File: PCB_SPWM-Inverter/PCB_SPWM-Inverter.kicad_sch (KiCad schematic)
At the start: 14 parts, among them J1 VAC, J2 VIN, Q1 IRFZ44NPBF, Q2 IRFZ44NPBF, Q3 IRFZ44NPBF, Q4 IRFZ44NPBF, U1 STM32F401, U2 LM2596, U3 TC4420EPA, U4 TC4420EPA, U5 TC4420EPA, U6 TC4420EPA

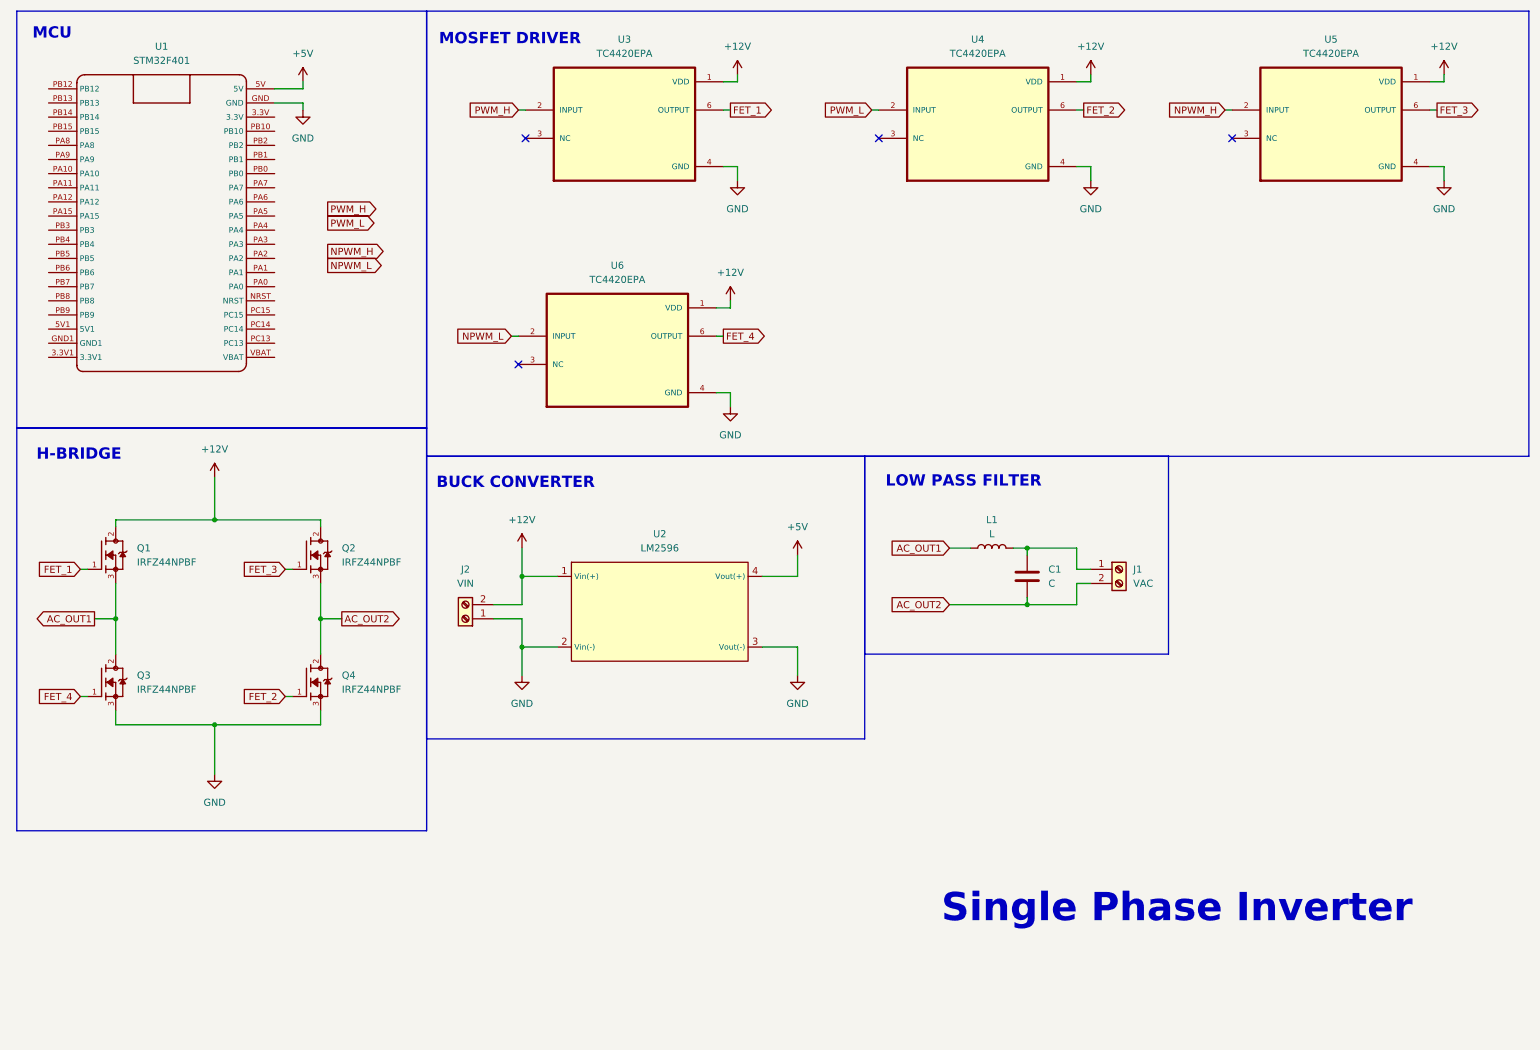
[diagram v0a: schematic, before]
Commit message: Add protection for H-bridge, calculate mosfet output, change mosfet driver to Half Bridge driver due to incompatibility on high side switching (unfinished)
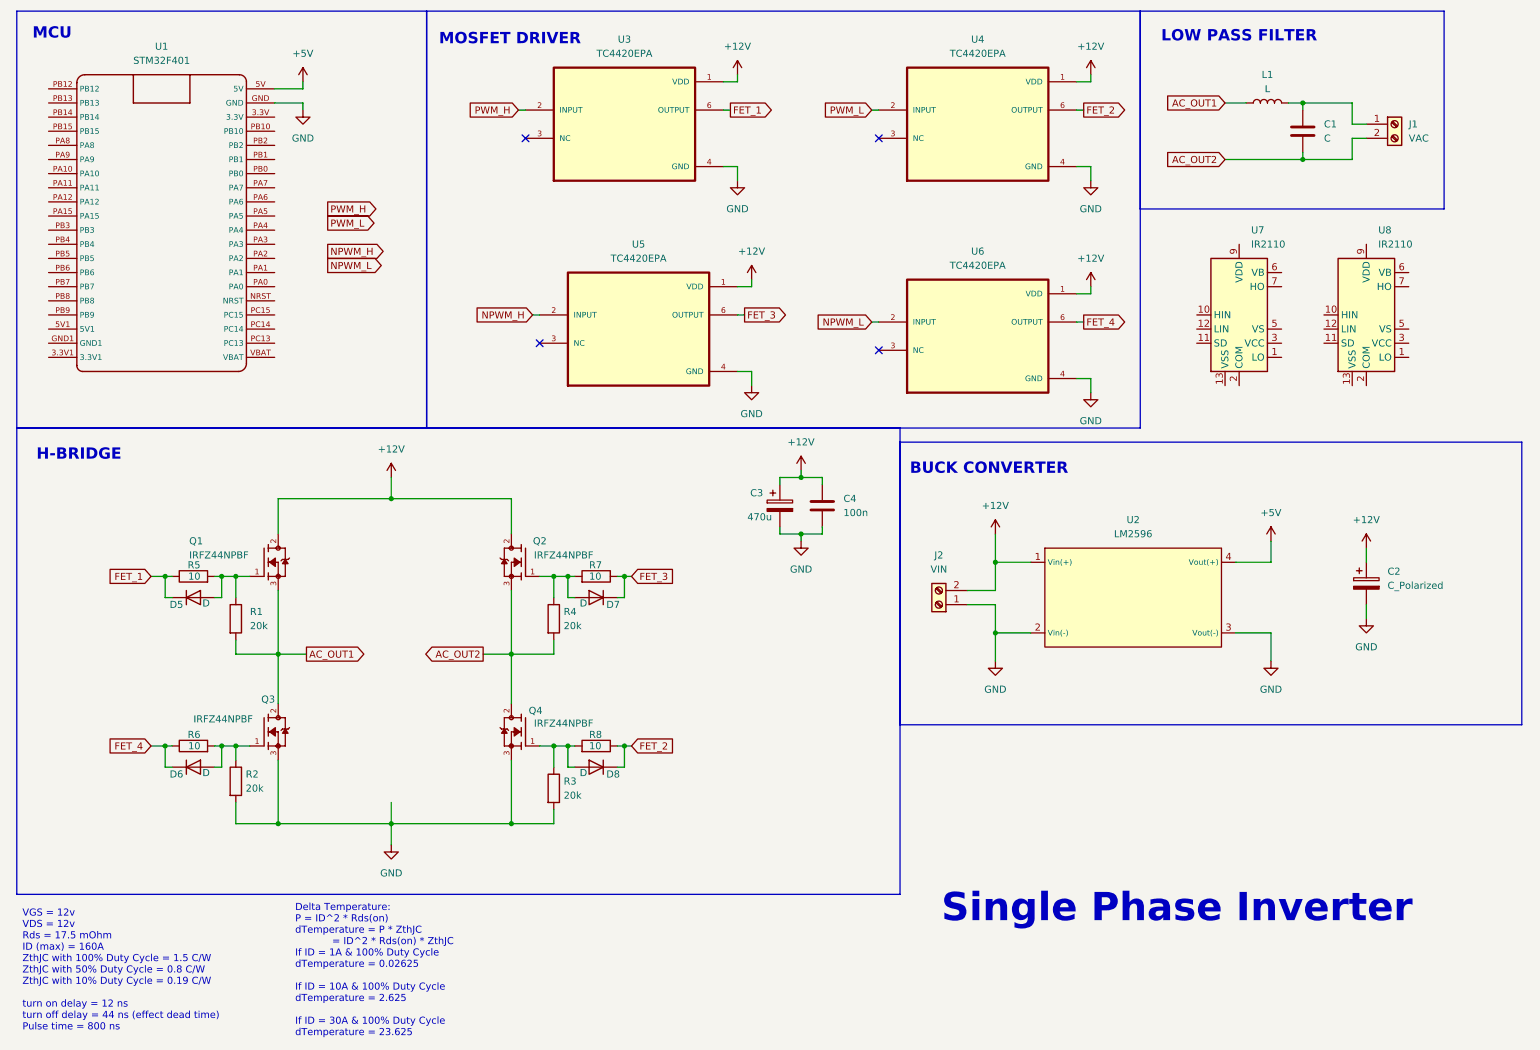
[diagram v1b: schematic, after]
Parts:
- added C2: C_Polarized, symbol Device:C_Polarized
- added C3: 470u, symbol Device:C_Polarized
- added C4: 100n, symbol Device:C
- added D5, D6, D7, D8: D, symbol Device:D
- added R1, R2, R3, R4: 20k, symbol Device:R
- added R5, R6, R7, R8: 10, symbol Device:R
- added U7, U8: IR2110, Package_DIP:DIP-14_W7.62mm, symbol Driver_FET:IR2110
- Q1, Q2, Q3, Q4: footprint IRFZ44NPBF:TO254P1016X419X2286-3 -> Footprint:TO254P1016X419X2286-3
- U1: footprint Component:STM32_F401_RCT -> Footprint:STM32_F401_RCT
- U2: footprint (none) -> Footprint:YAAJ_DCDC_StepDown_LM2596
- U3, U4, U5, U6: footprint TC4420EPA:DIP787W46P254L927H533Q8 -> Footprint:DIP787W46P254L927H533Q8
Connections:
- net +12V: now also C2.1, C3.1, C4.1
- net AC_OUT1: now also R1.2
- net AC_OUT2: now also R4.2
- net FET_1: now also D5.1 (K), R5.1; no longer Q1.1
- net FET_2: now also D8.1 (K), R8.1; no longer Q4.1
- net FET_3: now also D7.1 (K), R7.1; no longer Q2.1
- net FET_4: now also D6.1 (K), R6.1; no longer Q3.1
- net GND: now also C2.2, C3.2, C4.2, R2.2, R3.2
- new net: D8.2 (A), Q4.1, R3.1, R8.2
- new net: D7.2 (A), Q2.1, R4.1, R7.2
- new net: D6.2 (A), Q3.1, R2.1, R6.2
- new net: D5.2 (A), Q1.1, R1.1, R5.2
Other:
- note added: "Delta Temperature: P = ID^2 * Rds(on) dTemperature = P * ZthJC = ID^2 * Rds(on) * ZthJC If ID = 1A & 100% Duty Cycle dTemperature = 0.02625 If ID = 10A & 100% Duty Cycle dTemperature = 2.625 If ID = 30A & 100% Duty Cycle dTemperature = 23.625"
- note added: "VGS = 12v VDS = 12v Rds = 17.5 mOhm ID (max) = 160A ZthJC with 100% Duty Cycle = 1.5 C/W ZthJC with 50% Duty Cycle = 0.8 C/W ZthJC with 10% Duty Cycle = 0.19 C/W turn on delay = 12 ns turn off delay = 44 ns (effect dead time) Pulse time = 800 ns"
- moved on the sheet: C1, J1, J2, L1, Q1, Q2, Q3, Q4, U2, U5, U6

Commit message: Add circuit breaker and current sense. Assign footprint. Build half bridge driver circuit
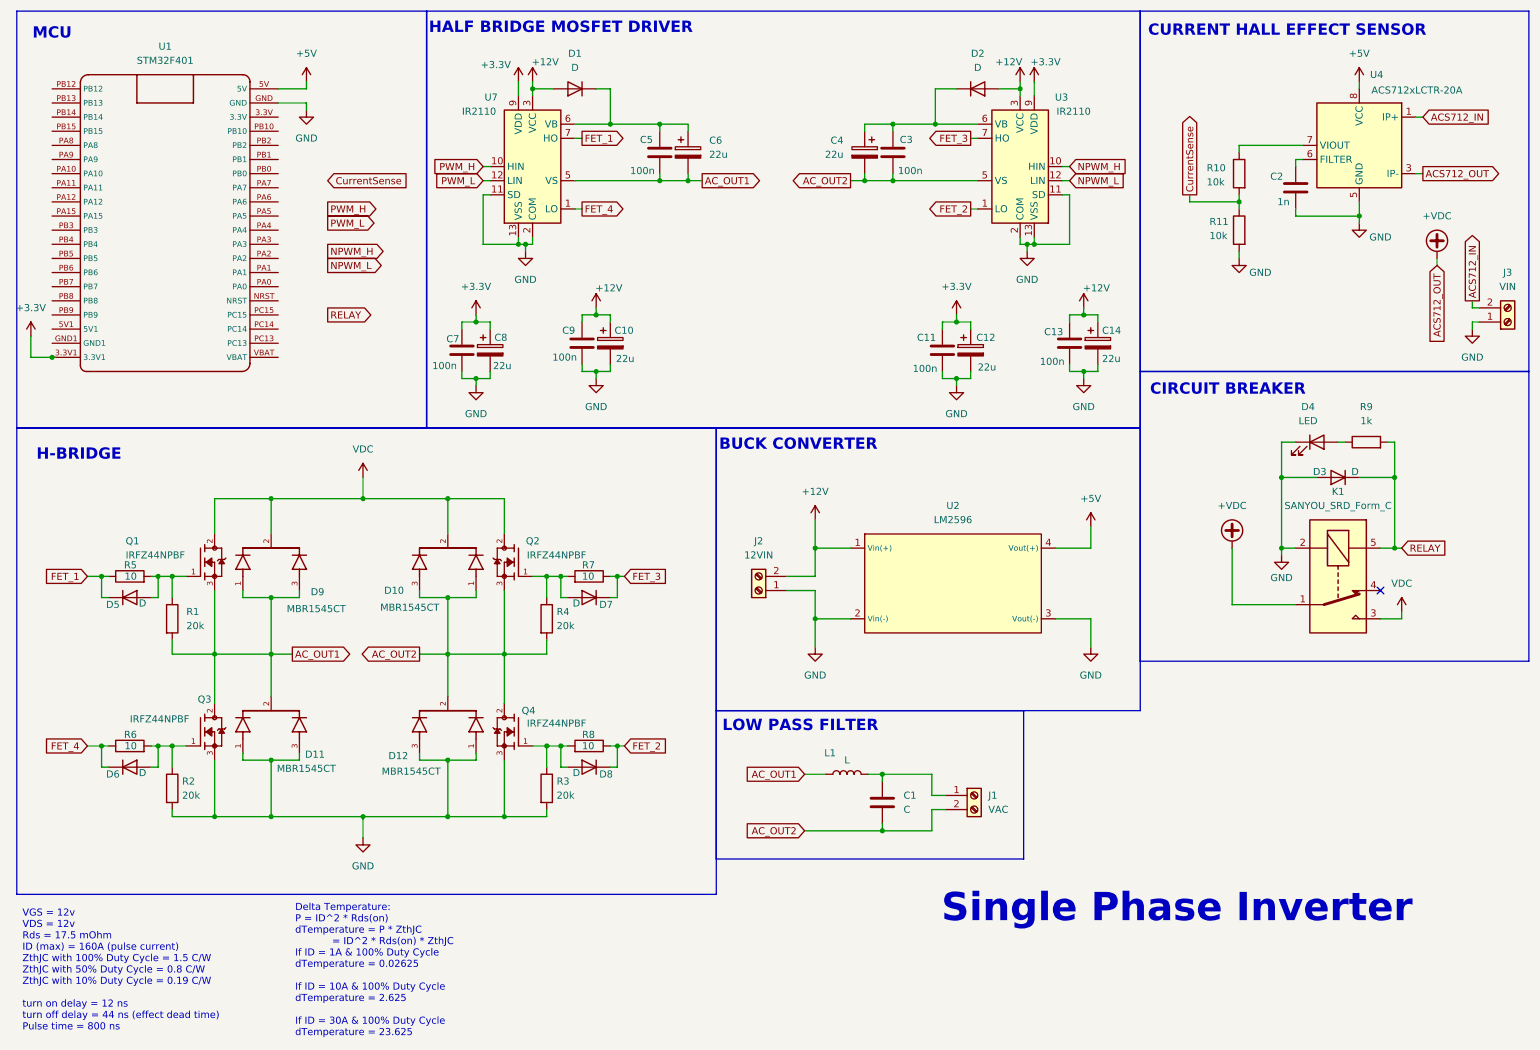
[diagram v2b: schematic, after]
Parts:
- removed C2: C_Polarized, symbol Device:C_Polarized
- removed C3: 470u, symbol Device:C_Polarized
- removed C4: 100n, symbol Device:C
- removed U3, U4, U5, U6: TC4420EPA, Footprint:DIP787W46P254L927H533Q8, symbol TC4420EPA:TC4420EPA
- removed U8: IR2110, Package_DIP:DIP-14_W7.62mm, symbol Driver_FET:IR2110
- added C10, C12, C14, C4, C6, C8: 22u, symbol Device:C_Polarized
- added C11, C13, C3, C5, C7, C9: 100n, symbol Device:C
- added C2: 1n, symbol Device:C
- added D1, D2, D3: D, Diode_THT:D_DO-41_SOD81_P10.16mm_Horizontal, symbol Device:D
- added D10, D11, D12, D9: MBR1545CT, Footprint:TO254P1050X476X2020-3, symbol MBR1545CT:MBR1545CT
- added D4: LED, symbol Device:LED
- added J3: VIN, symbol Connector:Screw_Terminal_01x02
- added K1: SANYOU_SRD_Form_C, Relay_THT:Relay_SPDT_SANYOU_SRD_Series_Form_C, symbol Relay:SANYOU_SRD_Form_C
- added R10, R11: 10k, Resistor_THT:R_Axial_DIN0207_L6.3mm_D2.5mm_P10.16mm_Horizontal, symbol Device:R
- added R9: 1k, Resistor_THT:R_Axial_DIN0207_L6.3mm_D2.5mm_P10.16mm_Horizontal, symbol Device:R
- added U3: IR2110, Package_DIP:DIP-14_W7.62mm, symbol Driver_FET:IR2110
- added U4: ACS712xLCTR-20A, Package_SO:SOIC-8_3.9x4.9mm_P1.27mm, symbol Sensor_Current:ACS712xLCTR-20A
- D5, D6, D7, D8: footprint (none) -> Diode_THT:D_DO-41_SOD81_P10.16mm_Horizontal
- J2: value VIN -> 12VIN
- R1, R2, R3, R4, R5, R6, R7, R8: footprint (none) -> Resistor_THT:R_Axial_DIN0207_L6.3mm_D2.5mm_P10.16mm_Horizontal
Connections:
- net +12V: now also U7.3 (VCC), C10.1, C13.1, C14.1, C9.1, D1.2 (A), D2.2 (A), U3.3 (VCC); no longer Q1.2, Q2.2
- net +5V: now also U4.8 (VCC)
- net AC_OUT1: now also U7.5 (VS), C5.2, C6.2, D11.2, D9.1, D9.3
- net AC_OUT2: now also C3.2, C4.2, D10.1, D10.3, D12.2, U3.5 (VS)
- net FET_1: now also U7.7 (HO)
- net FET_2: now also U3.1 (LO)
- net FET_3: now also U3.7 (HO)
- net FET_4: now also U7.1 (LO)
- net GND: now also U7.11 (SD), U7.13 (VSS), U7.2 (COM), C10.2, C11.2, C12.2, C13.2, C14.2, C2.2, C7.2, C8.2, C9.2, D11.1, D11.3, D12.1, D12.3, D3.2 (A), D4.1 (K), J3.1 (Pin_1), K1.2, R11.2, U3.11 (SD), U3.13 (VSS), U3.2 (COM), U4.5 (GND)
- net NPWM_H: now also U3.10 (HIN)
- net NPWM_L: now also U3.12 (LIN)
- net PWM_H: now also U7.10 (HIN)
- net PWM_L: now also U7.12 (LIN)
- net at U7.6 (VB): now also C5.1, C6.1, D1.1 (K)
- net +3.3V: now reaches U7.9 (VDD)
- net +3.3V: now also U1.3.3V1, C11.1, C12.1, C7.1, C8.1, U3.9 (VDD)
- new net: D4.2 (A), R9.1
- new net: C2.1, U4.6 (FILTER)
- new net: R10.1, U4.7 (VIOUT)
- new net: C3.1, C4.1, D2.1 (K), U3.6 (VB)
- new net +VDC: K1.1, U4.3 (IP-), U4.4 (IP-)
- new net ACS712_IN: J3.2 (Pin_2), U4.1 (IP+), U4.2 (IP+)
- new net CurrentSense: R10.2, R11.1
- new net RELAY: D3.1 (K), K1.5, R9.2
- new net VDC: D10.2, D9.2, K1.3, Q1.2, Q2.2
- no-connect marks 4 -> 1
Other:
- note added: "CIRCUIT BREAKER"
- note added: "CURRENT HALL EFFECT SENSOR"
- note added: "HALF BRIDGE MOSFET DRIVER"
- note added: "VGS = 12v VDS = 12v Rds = 17.5 mOhm ID (max) = 160A (pulse current) ZthJC with 100% Duty Cycle = 1.5 C/W ZthJC with 50% Duty Cycle = 0.8 C/W ZthJC with 10% Duty Cycle = 0.19 C/W turn on delay = 12 ns turn off delay = 44 ns (effect dead time) Pulse time = 800 ns"
- note removed: "MOSFET DRIVER"
- note removed: "VGS = 12v VDS = 12v Rds = 17.5 mOhm ID (max) = 160A ZthJC with 100% Duty Cycle = 1.5 C/W ZthJC with 50% Duty Cycle = 0.8 C/W ZthJC with 10% Duty Cycle = 0.19 C/W turn on delay = 12 ns turn off delay = 44 ns (effect dead time) Pulse time = 800 ns"
- moved on the sheet: C1, D5, D6, D7, D8, J1, J2, L1, Q1, Q2, Q3, Q4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
